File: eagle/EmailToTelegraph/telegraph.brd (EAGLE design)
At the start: 42.9 x 22.9 mm, 8 parts, among them Q1 MPSA42

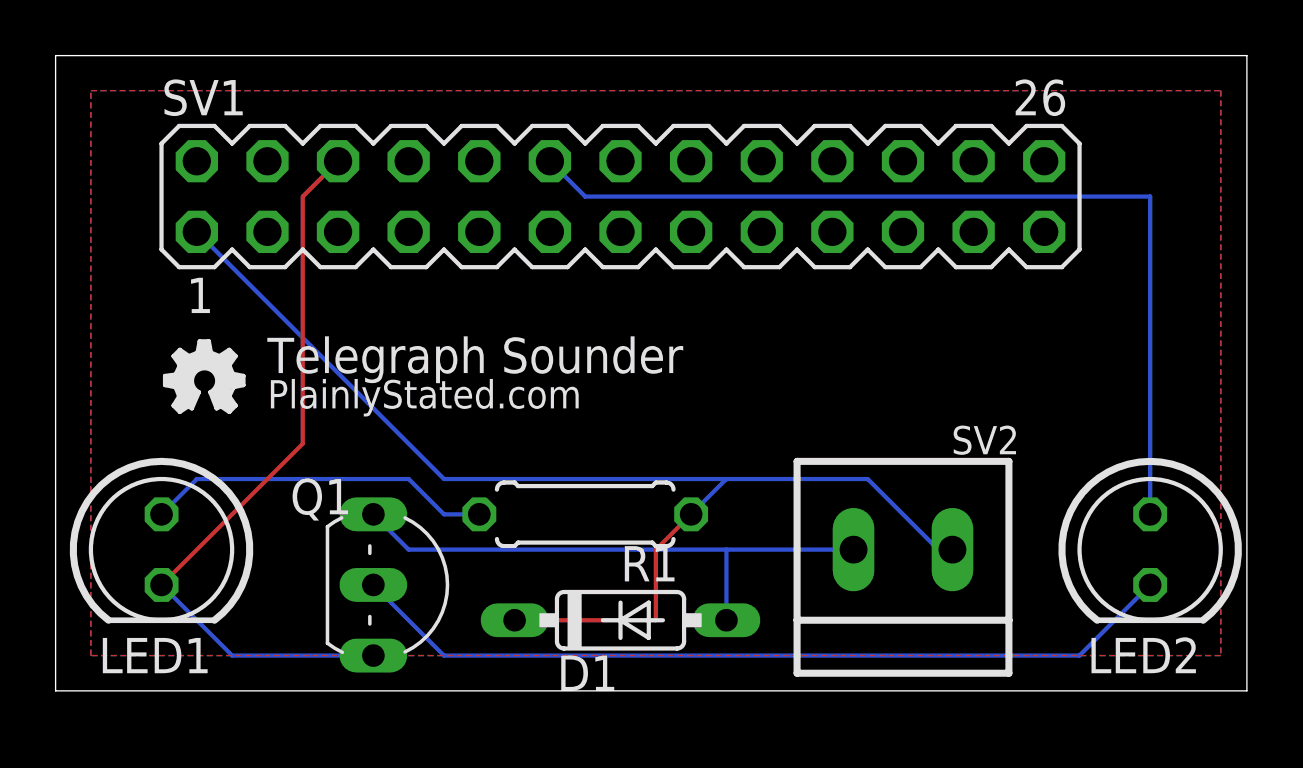
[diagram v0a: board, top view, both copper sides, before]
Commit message: reverse the orientation of the GPIO socket
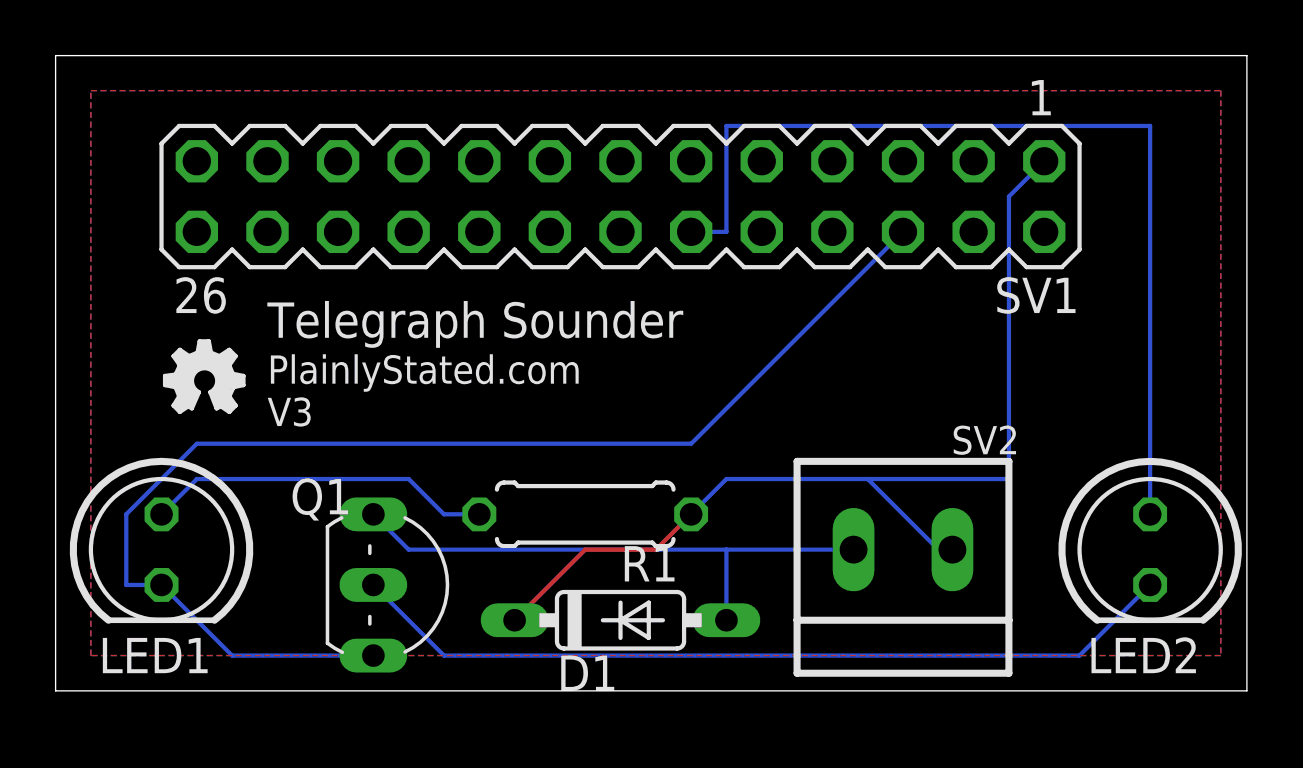
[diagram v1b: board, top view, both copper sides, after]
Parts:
- turned SV1 to 180 degrees
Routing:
- net N$4: track 26.5 -> 44.6 mm
- net N$6: track 43.1 -> 35.9 mm
- net N$7: track 33.5 -> 34.3 mm
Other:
- board text added: "PlainlyStated.com V3"
- board text removed: "PlainlyStated.com"
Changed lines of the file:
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@@
 <wire x1="42.85" y1="22.85" x2="0" y2="22.85" width="0" layer="20"/>
 <wire x1="0" y1="22.85" x2="0" y2="0" width="0" layer="20"/>
-<text x="7.62" y="11.43" size="1.27" layer="121">Telegraph Sounder</text>
-<text x="7.62" y="10.16" size="1.016" layer="121">PlainlyStated.com</text>
+<text x="7.62" y="12.7" size="1.27" layer="121">Telegraph Sounder</text>
+<text x="7.62" y="9.525" size="1.016" layer="121">PlainlyStated.com
+V3</text>
 </plain>
 <attributes>
@@
 </element>
 <element name="U$1" library="ohw-logo" package="OSHW_FILLX100_NOTEXT" value="" x="3.937" y="10.033"/>
-<element name="SV1" library="con-lstb" package="MA13-2" value="SV1" x="20.32" y="17.78">
-<attribute name="OC_NEWARK" value="unknown" x="20.32" y="17.78" size="1.778" layer="27" display="off"/>
-<attribute name="MPN" value="" x="20.32" y="17.78" size="1.778" layer="27" display="off"/>
-<attribute name="MF" value="" x="20.32" y="17.78" size="1.778" layer="27" display="off"/>
-<attribute name="OC_FARNELL" value="unknown" x="20.32" y="17.78" size="1.778" layer="27" display="off"/>
+<element name="SV1" library="con-lstb" package="MA13-2" value="SV1" x="20.32" y="17.78" rot="R180">
+<attribute name="OC_NEWARK" value="unknown" x="20.32" y="17.78" size="1.778" layer="27" rot="R180" display="off"/>
+<attribute name="MPN" value="" x="20.32" y="17.78" size="1.778" layer="27" rot="R180" display="off"/>
+<attribute name="MF" value="" x="20.32" y="17.78" size="1.778" layer="27" rot="R180" display="off"/>
+<attribute name="OC_FARNELL" value="unknown" x="20.32" y="17.78" size="1.778" layer="27" rot="R180" display="off"/>
 </element>
 <element name="SV2" library="plainlystated" package="HEADER2" value="HEADER2" x="30.48" y="5.08" smashed="yes" rot="R180">
@@
 <wire x1="6.35" y1="1.27" x2="3.81" y2="3.81" width="0.1524" layer="16"/>
 <wire x1="11.43" y1="1.27" x2="6.35" y2="1.27" width="0.1524" layer="16"/>
-<wire x1="8.89" y1="17.78" x2="10.16" y2="19.05" width="0.1524" layer="1"/>
-<wire x1="8.89" y1="8.89" x2="8.89" y2="17.78" width="0.1524" layer="1"/>
-<wire x1="3.81" y1="3.81" x2="8.89" y2="8.89" width="0.1524" layer="1"/>
+<wire x1="22.86" y1="8.89" x2="30.48" y2="16.51" width="0.1524" layer="16"/>
+<wire x1="5.08" y1="8.89" x2="22.86" y2="8.89" width="0.1524" layer="16"/>
+<wire x1="2.54" y1="6.35" x2="5.08" y2="8.89" width="0.1524" layer="16"/>
+<wire x1="2.54" y1="3.81" x2="2.54" y2="6.35" width="0.1524" layer="16"/>
+<wire x1="3.81" y1="3.81" x2="2.54" y2="3.81" width="0.1524" layer="16"/>
 </signal>
 <signal name="N$5">
@@
 <contactref element="LED2" pad="A"/>
 <contactref element="SV1" pad="12"/>
-<wire x1="39.37" y1="17.78" x2="39.37" y2="6.35" width="0.1524" layer="16"/>
-<wire x1="19.05" y1="17.78" x2="39.37" y2="17.78" width="0.1524" layer="16"/>
-<wire x1="17.78" y1="19.05" x2="19.05" y2="17.78" width="0.1524" layer="16"/>
+<wire x1="39.37" y1="20.32" x2="39.37" y2="6.35" width="0.1524" layer="16"/>
+<wire x1="24.13" y1="20.32" x2="39.37" y2="20.32" width="0.1524" layer="16"/>
+<wire x1="24.13" y1="16.51" x2="24.13" y2="20.32" width="0.1524" layer="16"/>
+<wire x1="22.86" y1="16.51" x2="24.13" y2="16.51" width="0.1524" layer="16"/>
 </signal>
 <signal name="N$3">
@@
 <contactref element="SV1" pad="1"/>
 <contactref element="SV2" pad="1"/>
-<wire x1="21.59" y1="2.54" x2="16.51" y2="2.54" width="0.1524" layer="1"/>
-<wire x1="21.59" y1="5.08" x2="21.59" y2="2.54" width="0.1524" layer="1"/>
+<wire x1="19.05" y1="5.08" x2="16.51" y2="2.54" width="0.1524" layer="1"/>
+<wire x1="21.59" y1="5.08" x2="19.05" y2="5.08" width="0.1524" layer="1"/>
 <wire x1="22.86" y1="6.35" x2="21.59" y2="5.08" width="0.1524" layer="1"/>
 <wire x1="29.21" y1="7.62" x2="31.75" y2="5.08" width="0.1524" layer="16"/>
@@
 <wire x1="22.86" y1="6.35" x2="24.13" y2="7.62" width="0.1524" layer="16"/>
 <wire x1="31.75" y1="5.08" x2="32.258" y2="5.08" width="0.1524" layer="16"/>
-<wire x1="13.97" y1="7.62" x2="5.08" y2="16.51" width="0.1524" layer="16"/>
-<wire x1="24.13" y1="7.62" x2="13.97" y2="7.62" width="0.1524" layer="16"/>
+<wire x1="34.29" y1="17.78" x2="35.56" y2="19.05" width="0.1524" layer="16"/>
+<wire x1="34.29" y1="7.62" x2="34.29" y2="17.78" width="0.1524" layer="16"/>
+<wire x1="29.21" y1="7.62" x2="34.29" y2="7.62" width="0.1524" layer="16"/>
 </signal>
 <signal name="N$2">
@@
 </board>
 </drawing>
+<compatibility>
+<note version="6.3" minversion="6.2.2" severity="warning">
+Since Version 6.2.2 text objects can contain more than one line,
+which will not be processed correctly with this version.
+</note>
+</compatibility>
 </eagle>
